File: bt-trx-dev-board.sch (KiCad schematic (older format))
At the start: 18 parts, among them J1 RJ45, J10 Conn_01x08, J2 PTT_BUTTON, J3 PTT_CON, J5 PTT_SEL, J9 Conn_01x08, U1 SILabs_WT32i, U2 LTV-816S

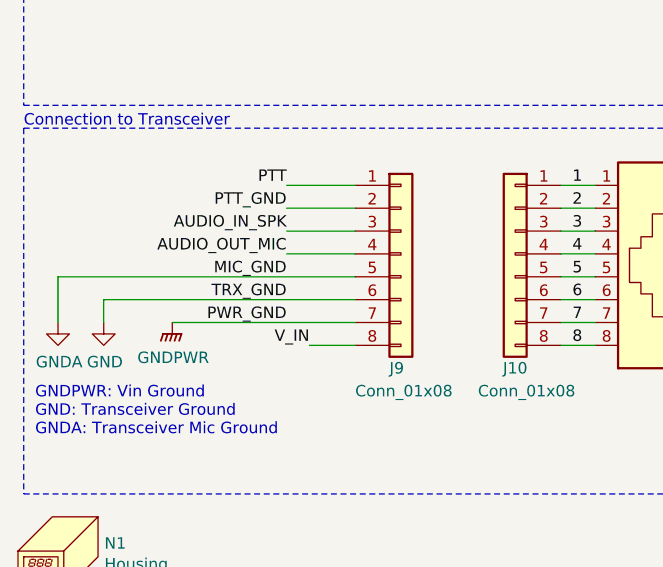
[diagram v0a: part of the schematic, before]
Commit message: Reworked PCB [#19][#21][#22][#23]
* Reworked PCB with new v5.0 schematic
* Fixed position of mounting holes
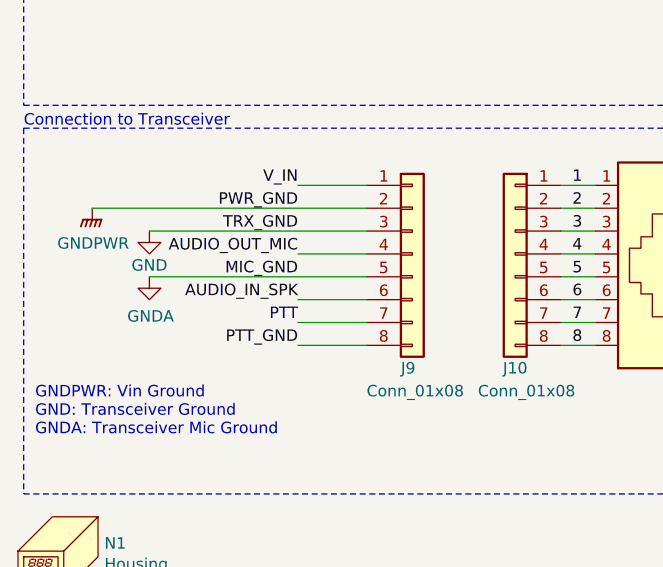
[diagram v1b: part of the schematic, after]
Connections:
- net AUDIO_IN_SPK: now also J9.6 (Pin_6); no longer J9.3 (Pin_3)
- net GND: now also J9.3 (Pin_3); no longer J9.6 (Pin_6)
- net GNDPWR: now also J9.2 (Pin_2); no longer J9.7 (Pin_7)
- net PTT: now also J9.7 (Pin_7); no longer J9.1 (Pin_1)
- net PTT_GND: now also J9.8 (Pin_8); no longer J9.2 (Pin_2)
- net V_IN: now also J9.1 (Pin_1); no longer J9.8 (Pin_8)
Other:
- moved on the sheet: J9
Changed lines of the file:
@@
 	4650 2450 5300 2450
 Wire Wire Line
-	2150 5350 1850 5350
-Text Label 1850 5050 2    50   ~ 0
+	2200 5350 1900 5350
+Text Label 1900 5650 2    50   ~ 0
 PTT
 Wire Wire Line
-	1850 5250 2150 5250
-Text Label 1850 5250 2    50   ~ 0
+	1900 5550 2200 5550
+Text Label 1900 5550 2    50   ~ 0
 AUDIO_IN_SPK
-Text Label 1850 5550 2    50   ~ 0
+Text Label 1900 5250 2    50   ~ 0
 TRX_GND
-Text Label 1850 5350 2    50   ~ 0
+Text Label 1900 5350 2    50   ~ 0
 AUDIO_OUT_MIC
-Wire Wire Line
-	1350 5650 2150 5650
-Text Label 1850 5650 2    50   ~ 0
+Text Label 1900 5150 2    50   ~ 0
 PWR_GND
-Text Label 1950 5750 2    50   ~ 0
+Text Label 1900 5050 2    50   ~ 0
 V_IN
-Text Label 1850 5450 2    50   ~ 0
+Text Label 1900 5450 2    50   ~ 0
 MIC_GND
 Text Notes 750  6150 0    50   ~ 0
@@
 L power:GNDPWR #PWR04
 U 1 1 5E273431
-P 1350 5650
-F 0 "#PWR04" H 1350 5450 50  0001 C CNN
-F 1 "GNDPWR" H 1354 5496 50  0000 C CNN
-F 2 "" H 1350 5600 50  0001 C CNN
-F 3 "" H 1350 5600 50  0001 C CNN
-	1    1350 5650
+P 1000 5150
+F 0 "#PWR04" H 1000 4950 50  0001 C CNN
+F 1 "GNDPWR" H 1004 4996 50  0000 C CNN
+F 2 "" H 1000 5100 50  0001 C CNN
+F 3 "" H 1000 5100 50  0001 C CNN
+	1    1000 5150
 	1    0    0    -1
 $EndComp
@@
 L power:GNDA #PWR01
 U 1 1 5E2852CB
-P 850 5650
-F 0 "#PWR01" H 850 5400 50  0001 C CNN
-F 1 "GNDA" H 855 5477 50  0000 C CNN
-F 2 "" H 850 5650 50  0001 C CNN
-F 3 "" H 850 5650 50  0001 C CNN
-	1    850  5650
+P 1250 5450
+F 0 "#PWR01" H 1250 5200 50  0001 C CNN
+F 1 "GNDA" H 1255 5277 50  0000 C CNN
+F 2 "" H 1250 5450 50  0001 C CNN
+F 3 "" H 1250 5450 50  0001 C CNN
+	1    1250 5450
 	1    0    0    -1
 $EndComp
@@
 L power:GND #PWR02
 U 1 1 5E30E15A
-P 1050 5650
-F 0 "#PWR02" H 1050 5400 50  0001 C CNN
-F 1 "GND" H 1055 5477 50  0000 C CNN
-F 2 "" H 1050 5650 50  0001 C CNN
-F 3 "" H 1050 5650 50  0001 C CNN
-	1    1050 5650
+P 1250 5250
+F 0 "#PWR02" H 1250 5000 50  0001 C CNN
+F 1 "GND" H 1250 5100 50  0000 C CNN
+F 2 "" H 1250 5250 50  0001 C CNN
+F 3 "" H 1250 5250 50  0001 C CNN
+	1    1250 5250
 	1    0    0    -1
 $EndComp
@@
 Wire Notes Line
 	6950 4150 6950 6400
-Wire Wire Line
-	1950 5750 2150 5750
-Wire Wire Line
-	1050 5650 1050 5550
-Wire Wire Line
-	1050 5550 2150 5550
-Wire Wire Line
-	850  5450 850  5650
-Wire Wire Line
-	850  5450 2150 5450
 $Comp
 L Connector_Generic:Conn_01x08 J9
 U 1 1 5E59CAEC
-P 2350 5350
-F 0 "J9" H 2300 4850 50  0000 L CNN
-F 1 "Conn_01x08" H 2150 4750 50  0000 L CNN
-F 2 "Connector_PinSocket_2.54mm:PinSocket_1x08_P2.54mm_Vertical" H 2350 5350 50  0001 C CNN
-F 3 "~" H 2350 5350 50  0001 C CNN
-	1    2350 5350
+P 2400 5350
+F 0 "J9" H 2350 4850 50  0000 L CNN
+F 1 "Conn_01x08" H 2200 4750 50  0000 L CNN
+F 2 "Connector_PinSocket_2.54mm:PinSocket_1x08_P2.54mm_Vertical" H 2400 5350 50  0001 C CNN
+F 3 "~" H 2400 5350 50  0001 C CNN
+	1    2400 5350
 	1    0    0    -1
 $EndComp
@@
 Wire Wire Line
 	8850 6050 8650 6050
-Text Label 1850 5150 2    50   ~ 0
+Text Label 1900 5750 2    50   ~ 0
 PTT_GND
 Wire Wire Line
-	1850 5050 2150 5050
-Wire Wire Line
-	2150 5150 1850 5150
+	1900 5650 2200 5650
+Wire Wire Line
+	2200 5750 1900 5750
 Text Label 10100 5750 0    50   ~ 0
 PTT_GND
@@
 Wire Notes Line
 	700  4800 700  6400
+Wire Wire Line
+	1250 5250 2200 5250
+Wire Wire Line
+	1250 5450 2200 5450
+Wire Wire Line
+	1000 5150 2200 5150
+Wire Wire Line
+	1900 5050 2200 5050
 $EndSCHEMATC

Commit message: BOM Update
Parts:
- J10: value Conn_01x08 -> JMP_CON_TRX; Mouser Best.Nr. (none) -> 855-M20-7820842
- J2, J3: DNA (none) -> DNA
- J9: value Conn_01x08 -> JMP_CON; Mouser Best.Nr. (none) -> 855-M20-7820842
- U2: Mouser Best.Nr. (none) -> 859-LTV-816S
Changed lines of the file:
@@
 F 3 "~" H 7250 5850 50  0001 C CNN
 F 4 "490-SJ1-3533NG" H 7250 5850 50  0001 C CNN "Mouser Best.Nr."
+F 5 "DNA" H 7250 5850 50  0001 C CNN "DNA"
 	1    7250 5850
 	1    0    0    1
@@
 F 3 "~" H 7100 5100 50  0001 C CNN
 F 4 "855-M20-9990346" H 200 -700 50  0001 C CNN "Mouser Best.Nr."
+F 5 "DNA" H 7100 5100 50  0001 C CNN "DNA"
 	1    7100 5100
 	-1   0    0    -1
@@
 F 2 "liteon:LTV-816S" H 9300 5450 50  0001 L CIN
 F 3 "https://www.mouser.de/datasheet/2/239/LTV-8x6-1175385.pdf" H 9500 5650 50  0001 L CNN
+F 4 " 859-LTV-816S " H 9500 5650 50  0001 C CNN "Mouser Best.Nr."
 	1    9500 5650
 	1    0    0    -1
@@
 P 2400 5350
 F 0 "J9" H 2350 4850 50  0000 L CNN
-F 1 "Conn_01x08" H 2200 4750 50  0000 L CNN
+F 1 "JMP_CON" H 2200 4750 50  0000 L CNN
 F 2 "Connector_PinSocket_2.54mm:PinSocket_1x08_P2.54mm_Vertical" H 2400 5350 50  0001 C CNN
 F 3 "~" H 2400 5350 50  0001 C CNN
+F 4 " 855-M20-7820842 " H 2400 5350 50  0001 C CNN "Mouser Best.Nr."
 	1    2400 5350
 	1    0    0    -1
@@
 P 2850 5350
 F 0 "J10" H 2850 4850 50  0000 C CNN
-F 1 "Conn_01x08" H 2800 4750 50  0000 C CNN
+F 1 "JMP_CON_TRX" H 2800 4750 50  0000 C CNN
 F 2 "Connector_PinSocket_2.54mm:PinSocket_1x08_P2.54mm_Vertical" H 2850 5350 50  0001 C CNN
 F 3 "~" H 2850 5350 50  0001 C CNN
+F 4 " 855-M20-7820842 " H 2850 5350 50  0001 C CNN "Mouser Best.Nr."
 	1    2850 5350
 	-1   0    0    -1

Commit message: Fixed mouser order IDs
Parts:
- C8, C9: Mouser Best.Nr. 80-C0805C105K3RAUTO -> 710-885012207098
- J10, J9: Mouser Best.Nr. 855-M20-7820842 -> 855-M20-7820842
- N1: Mouser Best.Nr. 546-1553CBKBAT -> 546-1553CBKBAT
- R1: Mouser Best.Nr. 603-RC0805FR-0710KL -> 603-RC0805FR-0710KL
- R8: Mouser Best.Nr. 603-RC0805FR-0710KL -> 603-RC0805FR-10220RL
- U2: Mouser Best.Nr. 859-LTV-816S -> 859-LTV-816S
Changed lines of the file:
@@
 F 2 "Symbol:OSHW-Logo2_7.3x6mm_SilkScreen" H 950 6700 50  0001 C CNN
 F 3 "~" H 950 6700 50  0001 C CNN
-F 4 " 546-1553CBKBAT " H 0   300 50  0001 C CNN "Mouser Best.Nr."
+F 4 "546-1553CBKBAT " H 0   300 50  0001 C CNN "Mouser Best.Nr."
 	1    900  6650
 	1    0    0    -1
@@
 F 2 "Resistor_SMD:R_0805_2012Metric_Pad1.15x1.40mm_HandSolder" V 7480 4750 50  0001 C CNN
 F 3 "~" H 7550 4750 50  0001 C CNN
-F 4 " 603-RC0805FR-0710KL" H 3900 -400 50  0001 C CNN "Mouser Best.Nr."
+F 4 "603-RC0805FR-0710KL" H 3900 -400 50  0001 C CNN "Mouser Best.Nr."
 	1    7550 4750
 	-1   0    0    1
@@
 F 2 "liteon:LTV-816S" H 9300 5450 50  0001 L CIN
 F 3 "https://www.mouser.de/datasheet/2/239/LTV-8x6-1175385.pdf" H 9500 5650 50  0001 L CNN
-F 4 " 859-LTV-816S " H 9500 5650 50  0001 C CNN "Mouser Best.Nr."
+F 4 "859-LTV-816S " H 9500 5650 50  0001 C CNN "Mouser Best.Nr."
 	1    9500 5650
 	1    0    0    -1
@@
 F 2 "Resistor_SMD:R_0805_2012Metric_Pad1.15x1.40mm_HandSolder" V 9030 5300 50  0001 C CNN
 F 3 "~" H 9100 5300 50  0001 C CNN
-F 4 " 603-RC0805FR-0710KL" H 5450 150 50  0001 C CNN "Mouser Best.Nr."
+F 4 "603-RC0805FR-10220RL" H 5450 150 50  0001 C CNN "Mouser Best.Nr."
 	1    9100 5300
 	1    0    0    -1
@@
 F 2 "Connector_PinSocket_2.54mm:PinSocket_1x08_P2.54mm_Vertical" H 2400 5350 50  0001 C CNN
 F 3 "~" H 2400 5350 50  0001 C CNN
-F 4 " 855-M20-7820842 " H 2400 5350 50  0001 C CNN "Mouser Best.Nr."
+F 4 "855-M20-7820842 " H 2400 5350 50  0001 C CNN "Mouser Best.Nr."
 	1    2400 5350
 	1    0    0    -1
@@
 F 2 "Connector_PinSocket_2.54mm:PinSocket_1x08_P2.54mm_Vertical" H 2850 5350 50  0001 C CNN
 F 3 "~" H 2850 5350 50  0001 C CNN
-F 4 " 855-M20-7820842 " H 2850 5350 50  0001 C CNN "Mouser Best.Nr."
+F 4 "855-M20-7820842 " H 2850 5350 50  0001 C CNN "Mouser Best.Nr."
 	1    2850 5350
 	-1   0    0    -1
@@
 F 2 "Capacitor_SMD:C_0805_2012Metric_Pad1.15x1.40mm_HandSolder" H 1788 3550 50  0001 C CNN
 F 3 "~" H 1750 3700 50  0001 C CNN
-F 4 "80-C0805C105K3RAUTO" H 0   -3150 50  0001 C CNN "Mouser Best.Nr."
+F 4 "710-885012207098" H 0   -3150 50  0001 C CNN "Mouser Best.Nr."
 	1    1750 3700
 	-1   0    0    1
@@
 F 2 "Capacitor_SMD:C_0805_2012Metric_Pad1.15x1.40mm_HandSolder" H 1338 3550 50  0001 C CNN
 F 3 "~" H 1300 3700 50  0001 C CNN
-F 4 "80-C0805C105K3RAUTO" H -450 -3150 50  0001 C CNN "Mouser Best.Nr."
+F 4 "710-885012207098" H -450 -3150 50  0001 C CNN "Mouser Best.Nr."
 	1    1300 3700
 	-1   0    0    1

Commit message: Add Digikey Part Numbers
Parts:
- C4: PartNrDigikey (none) -> 399-6929-1-ND
- C8, C9: PartNrDigikey (none) -> 732-8080-1-ND
- J1: PartNrDigikey (none) -> 609-1046-ND
- J10, J9: PartNrDigikey (none) -> 952-1823-ND
- J2, J5: PartNrDigikey (none) -> 952-2264-ND
- J3: PartNrDigikey (none) -> CP1-3533NG-ND
- N1: Mouser Best.Nr. 546-1553CBKBAT -> 546-1553CBK; PartNrDigikey (none) -> HM447-ND
- R1: PartNrDigikey (none) -> 311-10.0KCRCT-ND
- U1: PartNrDigikey (none) -> 336-3599-1-ND
- U2: PartNrDigikey (none) -> 160-1361-5-ND
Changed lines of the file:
@@
 EESchema Schematic File Version 4
+LIBS:bt-trx-dev-board-cache
 EELAYER 30 0
 EELAYER END
@@
 F 5 "Silicon Labs" H 2900 3850 50  0001 L BNN "Manufacturer"
 F 6 "634-WT32I-A-AI61" H 0   0   50  0001 C CNN "Mouser Best.Nr."
+F 7 "336-3599-1-ND" H 3750 2550 50  0001 C CNN "PartNrDigikey"
 	1    3750 2550
 	1    0    0    -1
@@
 F 3 "~" V 3600 5375 50  0001 C CNN
 F 4 "649-54602-908LF " H -6000 -400 50  0001 C CNN "Mouser Best.Nr."
+F 5 "609-1046-ND" H 3600 5350 50  0001 C CNN "PartNrDigikey"
 	1    3600 5350
 	-1   0    0    1
@@
 F 2 "Symbol:OSHW-Logo2_7.3x6mm_SilkScreen" H 950 6700 50  0001 C CNN
 F 3 "~" H 950 6700 50  0001 C CNN
-F 4 "546-1553CBKBAT " H 0   300 50  0001 C CNN "Mouser Best.Nr."
+F 4 "546-1553CBK" H 0   300 50  0001 C CNN "Mouser Best.Nr."
+F 5 "HM447-ND" H 900 6650 50  0001 C CNN "PartNrDigikey"
 	1    900  6650
 	1    0    0    -1
@@
 F 3 "~" H 7550 4750 50  0001 C CNN
 F 4 "603-RC0805FR-0710KL" H 3900 -400 50  0001 C CNN "Mouser Best.Nr."
+F 5 "311-10.0KCRCT-ND" H 7550 4750 50  0001 C CNN "PartNrDigikey"
 	1    7550 4750
 	-1   0    0    1
@@
 F 4 "490-SJ1-3533NG" H 7250 5850 50  0001 C CNN "Mouser Best.Nr."
 F 5 "DNA" H 7250 5850 50  0001 C CNN "DNA"
+F 6 "CP1-3533NG-ND" H 7250 5850 50  0001 C CNN "PartNrDigikey"
 	1    7250 5850
 	1    0    0    1
@@
 F 4 "855-M20-9990346" H 200 -700 50  0001 C CNN "Mouser Best.Nr."
 F 5 "DNA" H 7100 5100 50  0001 C CNN "DNA"
+F 6 "952-2264-ND" H 7100 5100 50  0001 C CNN "PartNrDigikey"
 	1    7100 5100
 	-1   0    0    -1
@@
 F 3 "https://www.mouser.de/datasheet/2/239/LTV-8x6-1175385.pdf" H 9500 5650 50  0001 L CNN
 F 4 "859-LTV-816S " H 9500 5650 50  0001 C CNN "Mouser Best.Nr."
+F 5 "160-1361-5-ND" H 9500 5650 50  0001 C CNN "PartNrDigikey"
 	1    9500 5650
 	1    0    0    -1
@@
 F 3 "~" H 5450 2450 50  0001 C CNN
 F 4 "80-C0805C105K3RAUTO" H 3700 -4400 50  0001 C CNN "Mouser Best.Nr."
+F 5 "399-6929-1-ND" H 5450 2450 50  0001 C CNN "PartNrDigikey"
 	1    5450 2450
 	0    1    1    0
@@
 F 3 "~" H 2400 5350 50  0001 C CNN
 F 4 "855-M20-7820842 " H 2400 5350 50  0001 C CNN "Mouser Best.Nr."
+F 5 "952-1823-ND" H 2400 5350 50  0001 C CNN "PartNrDigikey"
 	1    2400 5350
 	1    0    0    -1
@@
 F 3 "~" H 2850 5350 50  0001 C CNN
 F 4 "855-M20-7820842 " H 2850 5350 50  0001 C CNN "Mouser Best.Nr."
+F 5 "952-1823-ND" H 2850 5350 50  0001 C CNN "PartNrDigikey"
 	1    2850 5350
 	-1   0    0    -1
@@
 F 3 "~" H 8650 5750 50  0001 C CNN
 F 4 "855-M20-9990346" H 1750 -50 50  0001 C CNN "Mouser Best.Nr."
+F 5 "952-2264-ND" H 8650 5750 50  0001 C CNN "PartNrDigikey"
 	1    8650 5750
 	-1   0    0    -1
@@
 F 3 "~" H 1750 3700 50  0001 C CNN
 F 4 "710-885012207098" H 0   -3150 50  0001 C CNN "Mouser Best.Nr."
+F 5 "732-8080-1-ND" H 1750 3700 50  0001 C CNN "PartNrDigikey"
 	1    1750 3700
 	-1   0    0    1
@@
 F 3 "~" H 1300 3700 50  0001 C CNN
 F 4 "710-885012207098" H -450 -3150 50  0001 C CNN "Mouser Best.Nr."
+F 5 "732-8080-1-ND" H 1300 3700 50  0001 C CNN "PartNrDigikey"
 	1    1300 3700
 	-1   0    0    1
